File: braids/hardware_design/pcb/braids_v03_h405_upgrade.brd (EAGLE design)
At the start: 78.7 x 106.7 mm, 102 parts, among them IC1 74HC595D, IC2 74HC595D, IC3 DAC8551, IC4 LM1117-5.0, IC5 MCP6004, IC6 LM4040B25, IC7 LM4040B10, IC8 TL072, J1 PJ301_THONKICONN6, J2 PJ301_THONKICONN6, J3 PJ301_THONKICONN6, J4 PJ301_THONKICONN6, J5 PJ301_THONKICONN6, J6 PJ301_THONKICONN6, Q1 MMBT3904, Q2 MMBT3904, Q3 MMBT3904, Q4 MMBT3904, Q5 MMBT3904, SW1 EC12E_SW, SW2 LP4OA1PBCT

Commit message: Final tweaks
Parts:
- moved C11 0.95 mm to (41.6, 19.1)
- moved R31 0.95 mm to (41.6, 17.5)
- moved IC7 0.63 mm to (41.6, 14.9)
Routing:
- net AREF_-10: track 33.6 -> 34.2 mm
- net GND: vias 92 -> 91
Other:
- board text added: "Ah, buckle this!"
- board text removed: "Buckle up..."
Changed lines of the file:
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@@
 <text x="47.625" y="49.8475" size="0.8128" layer="25" font="vector" rot="R180">UART_TX</text>
 <rectangle x1="71.755" y1="13.97" x2="78.105" y2="14.605" layer="26"/>
-<text x="4.1275" y="71.4375" size="1.778" layer="25">Buckle up...</text>
-<text x="20.955" y="71.4375" size="1.778" layer="26" rot="MR0">Buckle up...</text>
+<text x="4.1275" y="71.4375" size="1.27" layer="25">Ah, buckle this!</text>
+<text x="20.955" y="71.4375" size="1.4224" layer="26" rot="MR0">Ah, buckle this!</text>
 </plain>
 <attributes>
@@
 <element name="R48" library="pot-alps" package="ALPS_POT_VERTICAL_PS" value="10kB" x="66.04" y="36.195" locked="yes" rot="R180"/>
 <element name="Q5" library="transistor" package="SOT23-BEC" value="MMBT3904" x="31.115" y="32.0675" smashed="yes">
-<attribute name="NAME" x="33.3375" y="30.48" size="0.8128" layer="25" font="vector"/>
-<attribute name="VALUE" x="33.3375" y="29.5275" size="0.6096" layer="27" font="vector"/>
+<attribute name="NAME" x="33.3375" y="31.75" size="0.8128" layer="25" font="vector"/>
+<attribute name="VALUE" x="33.3375" y="30.7975" size="0.6096" layer="27" font="vector"/>
 </element>
 <element name="R22" library="rcl" package="R0805" value="100k" x="31.115" y="28.8925" smashed="yes">
-<attribute name="NAME" x="29.845" y="26.9875" size="0.8128" layer="25" font="vector"/>
-<attribute name="VALUE" x="29.845" y="26.035" size="0.8128" layer="27" font="vector"/>
+<attribute name="NAME" x="33.02" y="29.21" size="0.8128" layer="25" font="vector"/>
+<attribute name="VALUE" x="33.02" y="28.2575" size="0.8128" layer="27" font="vector"/>
 </element>
 <element name="R23" library="rcl" package="R0805" value="10k" x="31.115" y="34.925" smashed="yes" rot="R180">
@@
 </element>
 <element name="MCU1" library="olimex-stm32h" package="STM32H103" value="STM32H405" x="39.37" y="49.53" smashed="yes" rot="MR180">
-<attribute name="NAME" x="36.83" y="33.02" size="1.27" layer="22" rot="MR180"/>
+<attribute name="NAME" x="37.1475" y="46.0375" size="1.27" layer="22" rot="MR180"/>
 <attribute name="VALUE" x="44.7675" y="42.545" size="1.27" layer="22" rot="MR0"/>
 </element>
-<element name="IC7" library="texas" package="DBZ_R-PDSO-G3" value="LM4040B10" x="41.5925" y="15.5575" smashed="yes" rot="R180">
-<attribute name="NAME" x="39.6875" y="14.605" size="0.8128" layer="25" font="vector" rot="R90"/>
-<attribute name="VALUE" x="39.6875" y="13.335" size="0.6096" layer="27" font="vector"/>
-</element>
-<element name="R31" library="rcl" package="R0603" value="470" x="41.5925" y="18.415" smashed="yes" rot="R180">
-<attribute name="NAME" x="40.005" y="19.05" size="0.8128" layer="25" rot="R180"/>
-<attribute name="VALUE" x="40.005" y="18.0975" size="0.8128" layer="27" rot="R180"/>
-</element>
-<element name="C11" library="rcl" package="C0603" value="100n" x="41.5925" y="20.0025" smashed="yes">
-<attribute name="NAME" x="40.64" y="21.9075" size="0.8128" layer="25"/>
-<attribute name="VALUE" x="40.64" y="20.955" size="0.8128" layer="27"/>
+<element name="IC7" library="texas" package="DBZ_R-PDSO-G3" value="LM4040B10" x="41.5925" y="14.9225" smashed="yes" rot="R180">
+<attribute name="NAME" x="39.6875" y="13.97" size="0.8128" layer="25" font="vector" rot="R90"/>
+<attribute name="VALUE" x="39.6875" y="12.7" size="0.6096" layer="27" font="vector"/>
+</element>
+<element name="R31" library="rcl" package="R0603" value="470" x="41.5925" y="17.4625" smashed="yes" rot="R180">
+<attribute name="NAME" x="40.005" y="18.0975" size="0.8128" layer="25" rot="R180"/>
+<attribute name="VALUE" x="40.005" y="17.145" size="0.8128" layer="27" rot="R180"/>
+</element>
+<element name="C11" library="rcl" package="C0603" value="100n" x="41.5925" y="19.05" smashed="yes">
+<attribute name="NAME" x="40.64" y="20.955" size="0.8128" layer="25"/>
+<attribute name="VALUE" x="40.64" y="20.0025" size="0.8128" layer="27"/>
 </element>
 <element name="JP1" library="og-header" package="AVR_ICSP" value="M05X2PTH" x="74.93" y="21.2725" smashed="yes"/>
@@
 <via x="60.325" y="19.685" extent="1-16" drill="0.6"/>
 <via x="49.53" y="21.2725" extent="1-16" drill="0.6"/>
-<via x="41.5925" y="12.7" extent="1-16" drill="0.6"/>
+<via x="41.5925" y="12.065" extent="1-16" drill="0.6"/>
 <contactref element="LED1" pad="K"/>
 <contactref element="S1" pad="1"/>
@@
 <via x="5.715" y="46.99" extent="1-16" drill="0.6"/>
 <via x="45.085" y="33.655" extent="1-16" drill="0.6"/>
-<via x="61.2775" y="29.5275" extent="1-16" drill="0.6"/>
 <via x="61.2775" y="32.0675" extent="1-16" drill="0.6"/>
 <via x="12.065" y="23.495" extent="1-16" drill="0.6"/>
@@
 <via x="31.75" y="76.835" extent="1-16" drill="0.6"/>
 <via x="33.655" y="69.215" extent="1-16" drill="0.6"/>
-<via x="70.8025" y="32.0675" extent="1-16" drill="0.6"/>
+<via x="71.12" y="31.4325" extent="1-16" drill="0.6"/>
 <via x="56.1975" y="43.815" extent="1-16" drill="0.6"/>
 <via x="34.6075" y="19.05" extent="1-16" drill="0.6"/>
@@
 <wire x1="56.515" y1="18.1" x2="55.1825" y2="18.1" width="0.4064" layer="1"/>
 <wire x1="55.1825" y1="18.1" x2="54.9275" y2="18.355" width="0.4064" layer="1"/>
-<wire x1="46.0375" y1="16.51" x2="44.1325" y2="18.415" width="0.4064" layer="16"/>
-<wire x1="44.1325" y1="18.415" x2="43.815" y2="18.415" width="0.4064" layer="16"/>
-<via x="43.815" y="18.415" extent="1-16" drill="0.6"/>
-<wire x1="43.815" y1="18.415" x2="42.4425" y2="18.415" width="0.4064" layer="1"/>
+<wire x1="45.085" y1="16.51" x2="44.1325" y2="17.4625" width="0.4064" layer="16"/>
+<via x="44.1325" y="17.4625" extent="1-16" drill="0.6"/>
+<wire x1="44.1325" y1="17.4625" x2="42.4425" y2="17.4625" width="0.4064" layer="1"/>
 <wire x1="56.515" y1="18.1" x2="56.515" y2="17.145" width="0.4064" layer="1"/>
 <wire x1="56.515" y1="17.145" x2="57.15" y2="16.51" width="0.4064" layer="1"/>
 <via x="57.15" y="16.51" extent="1-16" drill="0.6"/>
-<wire x1="57.15" y1="16.51" x2="46.0375" y2="16.51" width="0.4064" layer="16"/>
+<wire x1="57.15" y1="16.51" x2="45.085" y2="16.51" width="0.4064" layer="16"/>
 <wire x1="57.15" y1="16.51" x2="60.7825" y2="16.51" width="0.4064" layer="1"/>
 <wire x1="60.7825" y1="16.51" x2="61.1" y2="16.1925" width="0.4064" layer="1"/>
@@
 <wire x1="18.095" y1="21.2725" x2="18.095" y2="19.3675" width="0.4064" layer="1"/>
 <wire x1="36.5125" y1="21.27" x2="36.51" y2="21.2725" width="0.4064" layer="1"/>
-<wire x1="40.7425" y1="18.415" x2="40.7425" y2="20.0025" width="0.4064" layer="1"/>
-<wire x1="40.7425" y1="18.415" x2="40.7425" y2="16.7575" width="0.4064" layer="1"/>
-<wire x1="40.7425" y1="16.7575" x2="40.6425" y2="16.6575" width="0.4064" layer="1"/>
+<wire x1="40.7425" y1="17.4625" x2="40.7425" y2="19.05" width="0.4064" layer="1"/>
 <via x="39.37" y="20.32" extent="1-16" drill="0.6"/>
 <wire x1="20.0025" y1="19.3675" x2="32.385" y2="19.3675" width="0.4064" layer="16"/>
 <wire x1="32.385" y1="19.3675" x2="33.3375" y2="20.32" width="0.4064" layer="16"/>
 <wire x1="20.0025" y1="19.3675" x2="18.095" y2="19.3675" width="0.4064" layer="1"/>
-<wire x1="39.37" y1="20.32" x2="39.6875" y2="20.0025" width="0.4064" layer="1"/>
-<wire x1="39.6875" y1="20.0025" x2="40.7425" y2="20.0025" width="0.4064" layer="1"/>
 <via x="36.5125" y="19.05" extent="1-16" drill="0.6"/>
 <wire x1="39.37" y1="20.32" x2="36.5125" y2="20.32" width="0.4064" layer="16"/>
@@
 <wire x1="36.5125" y1="17.46" x2="36.5125" y2="19.05" width="0.4064" layer="1"/>
 <wire x1="36.5125" y1="19.05" x2="36.5125" y2="20.32" width="0.4064" layer="16"/>
+<wire x1="40.7425" y1="17.4625" x2="40.6425" y2="17.78" width="0.4064" layer="1"/>
+<wire x1="40.6425" y1="17.78" x2="40.6425" y2="16.0225" width="0.4064" layer="1"/>
+<wire x1="39.37" y1="20.32" x2="39.4725" y2="20.32" width="0.4064" layer="1"/>
+<wire x1="39.4725" y1="20.32" x2="40.7425" y2="19.05" width="0.4064" layer="1"/>
 </signal>
 <signal name="+3V3_A">
@@
 <wire x1="28.8925" y1="24.13" x2="28.4734" y2="24.13" width="0.254" layer="1"/>
 <contactref element="MCU1" pad="EXT1-26"/>
-<wire x1="32.7025" y1="25.08" x2="38.1025" y2="25.08" width="0.254" layer="1"/>
-<wire x1="38.1025" y1="25.08" x2="38.4175" y2="24.765" width="0.254" layer="1"/>
-<wire x1="38.4175" y1="24.765" x2="43.815" y2="24.765" width="0.254" layer="1"/>
+<wire x1="32.7025" y1="25.08" x2="40.0075" y2="25.08" width="0.254" layer="1"/>
+<wire x1="40.0075" y1="25.08" x2="40.3225" y2="24.765" width="0.254" layer="1"/>
+<wire x1="40.3225" y1="24.765" x2="43.815" y2="24.765" width="0.254" layer="1"/>
 <wire x1="43.815" y1="24.765" x2="46.0375" y2="26.9875" width="0.254" layer="1"/>
 <via x="46.0375" y="26.9875" extent="1-16" drill="0.6"/>

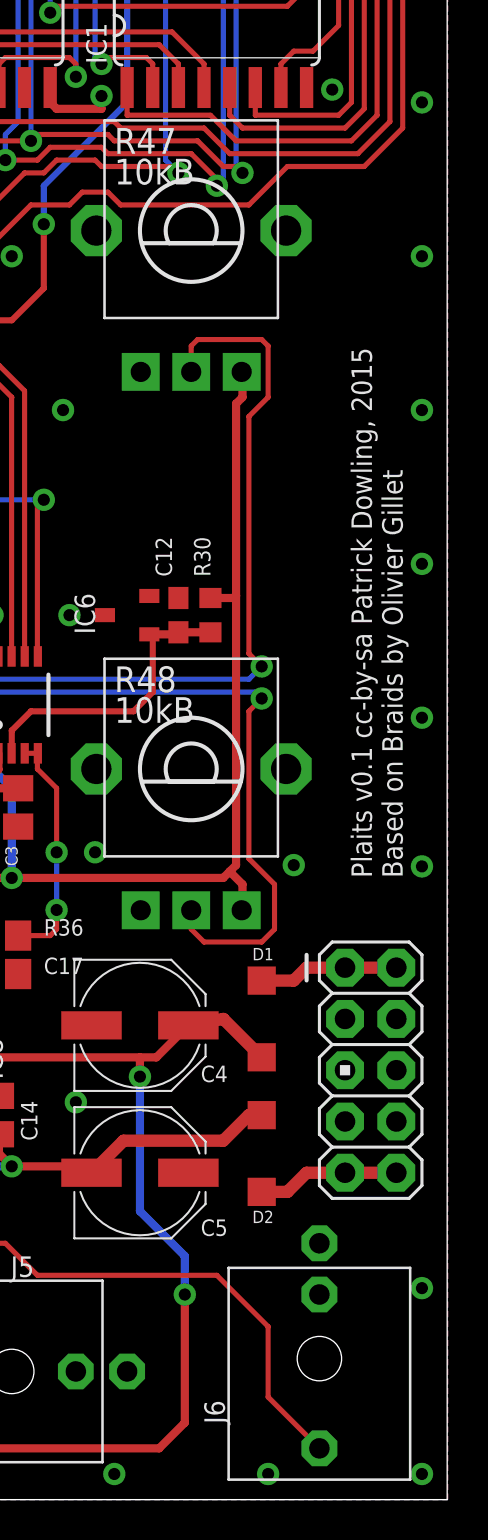
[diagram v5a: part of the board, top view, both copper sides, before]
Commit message: 0.2: Incorrectly placed audio jack
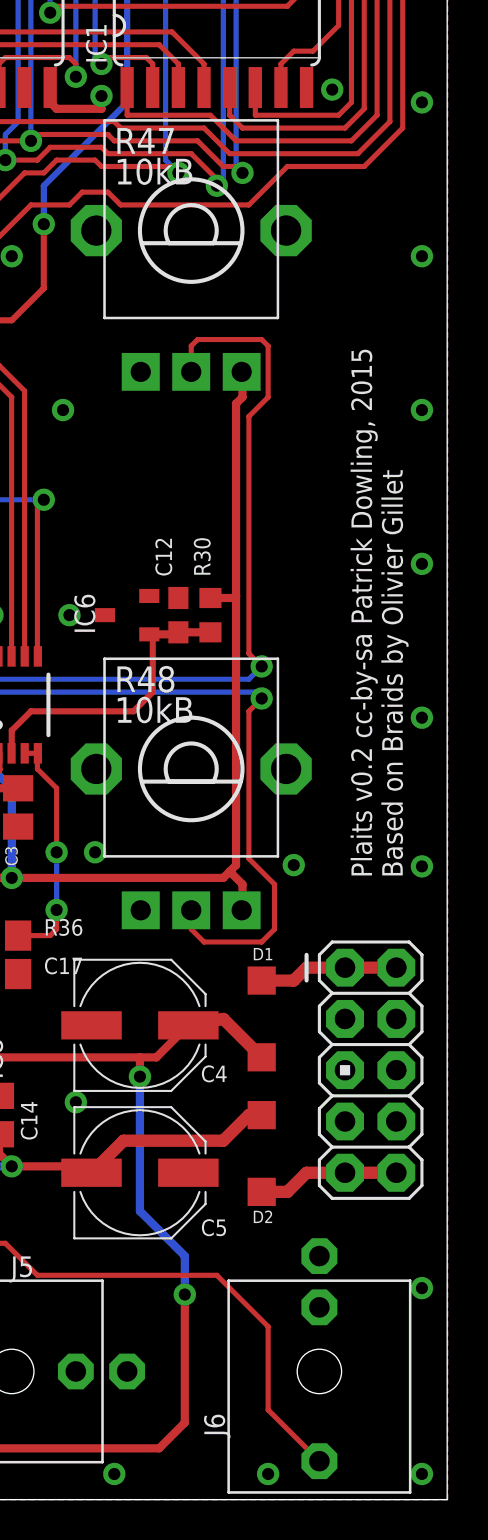
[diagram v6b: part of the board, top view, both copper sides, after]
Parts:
- moved J6 0.64 mm to (72.4, 6.35)
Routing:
- net N$72: track 30.2 -> 30.8 mm
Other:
- board text added: "Plaits v0.2 cc-by-sa Patrick Dowling, 2015 Based on Braids by Olivier Gillet"
- board text removed: "Plaits v0.1 cc-by-sa Patrick Dowling, 2015 Based on Braids by Olivier Gillet"
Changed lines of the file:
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@@
 <text x="70.485" y="23.495" size="1.016" layer="26" font="vector" ratio="15" rot="MR0">GND</text>
 <text x="4.1275" y="74.295" size="3.81" layer="25" font="vector" ratio="15">Plaits</text>
-<text x="76.5175" y="30.7975" size="1.016" layer="25" font="vector" ratio="15" rot="R90">Plaits v0.1 cc-by-sa Patrick Dowling, 2015
+<text x="76.5175" y="30.7975" size="1.016" layer="25" font="vector" ratio="15" rot="R90">Plaits v0.2 cc-by-sa Patrick Dowling, 2015
 Based on Braids by Olivier Gillet</text>
 <text x="76.5175" y="13.97" size="1.27" layer="26" font="vector" ratio="12" rot="MR270">Red stripe &gt;</text>
@@
 <text x="70.485" y="18.415" size="1.016" layer="26" font="vector" ratio="15" rot="MR0">GND</text>
 <text x="20.955" y="73.9775" size="3.81" layer="26" font="vector" ratio="15" rot="MR0">Plaits</text>
-<text x="73.9775" y="30.7975" size="1.016" layer="26" font="vector" ratio="15" rot="MR90">Plaits v0.1 cc-by-sa Patrick Dowling, 2015
+<text x="73.9775" y="30.7975" size="1.016" layer="26" font="vector" ratio="15" rot="MR90">Plaits v0.2 cc-by-sa Patrick Dowling, 2015
 Based on Braids by Olivier Gillet</text>
 <text x="47.625" y="52.3875" size="0.8128" layer="25" font="vector" rot="R180">DEBUG_PIN</text>
@@
 <attribute name="NAME" x="6.295" y="11.0325" size="1.016" layer="25"/>
 </element>
-<element name="J6" library="og-pj301" package="WQP_PJ_301M6" value="PJ301_THONKICONN6" x="72.39" y="6.985" locked="yes" smashed="yes" rot="R180">
-<attribute name="NAME" x="67.7075" y="3.755" size="1.016" layer="25" rot="R90"/>
+<element name="J6" library="og-pj301" package="WQP_PJ_301M6" value="PJ301_THONKICONN6" x="72.39" y="6.35" locked="yes" smashed="yes" rot="R180">
+<attribute name="NAME" x="67.7075" y="3.12" size="1.016" layer="25" rot="R90"/>
 </element>
 <element name="J4" library="og-pj301" package="WQP_PJ_301M6" value="PJ301_THONKICONN6" x="44.45" y="6.35" smashed="yes" rot="R90">
@@
 <contactref element="J6" pad="P3"/>
 <wire x1="67.31" y1="11.1125" x2="69.85" y2="8.5725" width="0.254" layer="1"/>
-<wire x1="69.85" y1="8.5725" x2="69.85" y2="5.08" width="0.254" layer="1"/>
-<wire x1="69.85" y1="5.08" x2="72.39" y2="2.54" width="0.254" layer="1"/>
+<wire x1="69.85" y1="8.5725" x2="69.85" y2="4.445" width="0.254" layer="1"/>
+<wire x1="69.85" y1="4.445" x2="72.39" y2="1.905" width="0.254" layer="1"/>
 <wire x1="50.8" y1="13.9725" x2="50.8" y2="13.0175" width="0.254" layer="1"/>
 <wire x1="50.8" y1="13.0175" x2="51.1175" y2="12.7" width="0.254" layer="1"/>

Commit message: Board tweaks
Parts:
- added R49: 100k, rcl:R1206
- C11, C12, C8: device rcl:C0603 -> rcl:C0805
- R1, R30, R31: device rcl:R0603 -> rcl:R0805
- moved IC6 0.64 mm to (62.2, 43.8)
- moved C11 0.45 mm to (41.3, 19.4)
- moved IC7 0.45 mm to (41.3, 14.6)
- moved R31 0.32 mm to (41.3, 17.5)
- moved C12 0.32 mm to (65.1, 43.8)
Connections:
- new net N$7: C6.+, IC4.2, R49.1
- net VCC: now also R49.2; no longer C6.+, IC4.2
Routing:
- net VCC: track 147.8 -> 134.3 mm
- net N$7: track 0.00 -> 11.8 mm
